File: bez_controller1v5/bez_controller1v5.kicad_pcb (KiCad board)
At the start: 4 copper layers, 110 x 65 mm, 88 parts, among them J1 Conn_01x03_Male, J10 Conn_01x07_Socket, J11 Conn_01x03_Male, J12 Conn_01x03_Male, J13 USB_B_Mini, J14 PPTC041LGBN-RC, J15 Conn_01x03_Male, J16 MOLEX_Conn_Button, J17 MOLEX_Conn_Button, J2 Conn_01x03_Male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

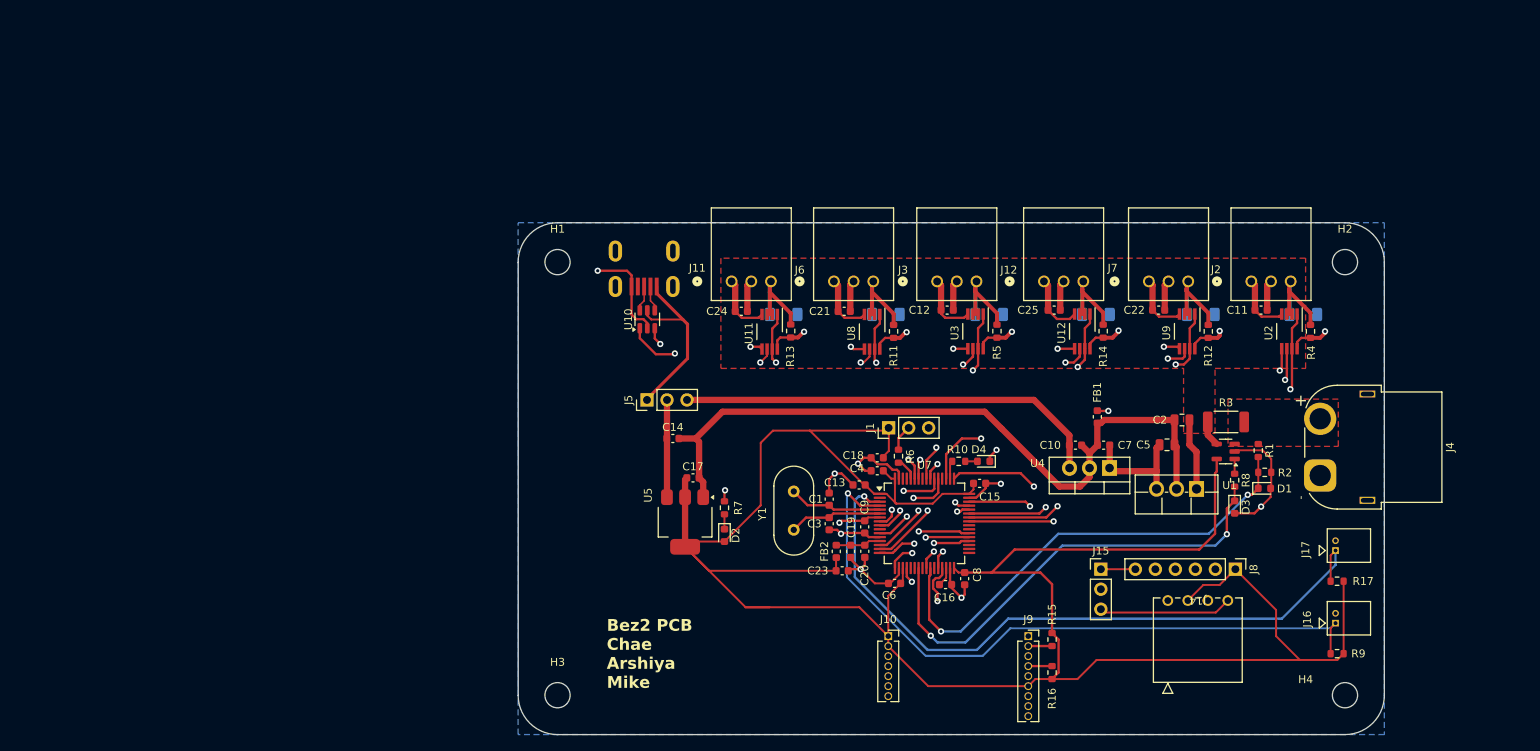
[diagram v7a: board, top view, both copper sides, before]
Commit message: -added label on each motor connections, -thickened 3.3v wires, removed uart line squiggles, updated U1 12v to 6v dcdc converter to new pxo7806-500
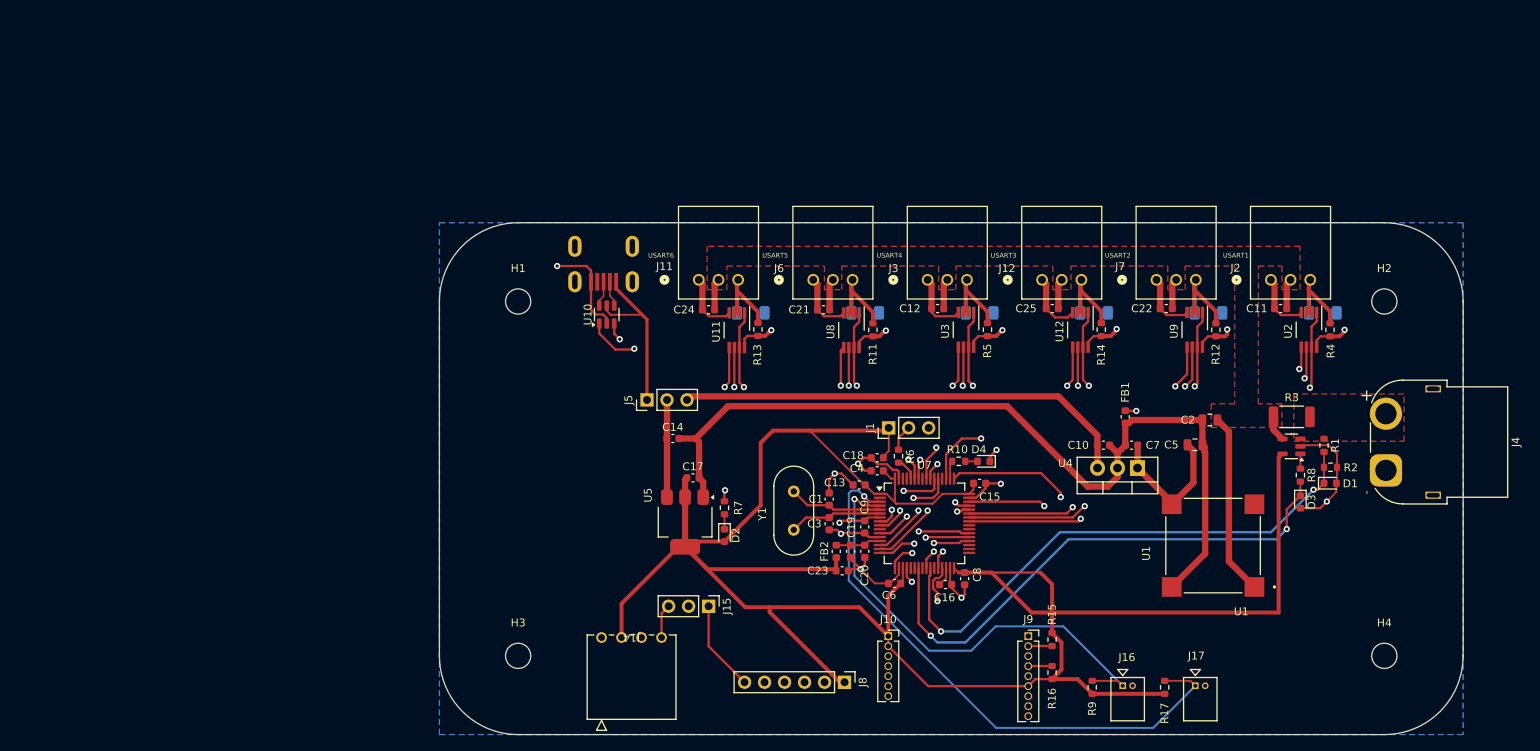
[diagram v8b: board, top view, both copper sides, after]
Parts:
- U1: value PX07806-500-S -> ~; footprint Package_TO_SOT_THT:TO-220F-3_Vertical -> KiCad:CONV_PXO7806-500-M-TR
- moved J14 72.1 mm to (104.3, 95.7)
- moved J8 51.7 mm to (135.2, 101.3)
- moved J15 50.0 mm to (117.9, 91.7), turned to -90 degrees
- moved R9 31.4 mm to (166.7, 102.0), turned to 90 degrees
- moved J16 28.2 mm to (170.5, 101.8), turned to 0 degrees
- moved R17 25.7 mm to (175.8, 102.0), turned to 90 degrees
- moved J17 24.7 mm to (179.8, 101.8), turned to 0 degrees
- moved R3 8.38 mm to (192.0, 67.7)
- moved D1 8.38 mm to (196.9, 76.1)
- moved D3 8.38 mm to (193.1, 78.5)
- moved J4 8.38 mm to (203.9, 74.5)
- moved R1 8.38 mm to (196.1, 71.3)
- moved R2 8.38 mm to (196.9, 74.0)
- moved R8 8.38 mm to (193.1, 75.0)
- moved U6 8.38 mm to (191.9, 71.4)
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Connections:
- U1 pad 2: /PWR_GND -> (no net)
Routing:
- net /GPIO1: track 87.4 -> 60.0 mm
- net /NRST: track 55.2 -> 29.6 mm
- net /TMS: track 31.3 -> 52.5 mm
- net /Screen_SCL: track 42.5 -> 61.3 mm
- net /PWR_GND: track 93.4 -> 111.7 mm
- net /TCK: track 41.0 -> 56.2 mm
- net /GPIO2: track 88.8 -> 73.9 mm
- net /post_shunt_12v: track 35.7 -> 49.8 mm
- net /SWO_or_Screen_SDA: track 32.7 -> 45.5 mm
- net /Screen_SDA: track 16.9 -> 4.35 mm
- net /V_bat_read: track 60.5 -> 69.1 mm
- net /V_shunt_read: track 59.3 -> 67.5 mm
- net /SWO: track 4.38 -> 11.5 mm
- net +3.3V: track 306.3 -> 299.7 mm
- net /USB_D+: track 58.0 -> 63.4 mm
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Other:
- board size 110 x 65 mm -> 130 x 65 mm
- board text added: "U1"
- board text added: "USART1"
- board text added: "USART2"
- board text added: "USART3"
- board text added: "USART4"
- board text added: "USART5"
- board text added: "USART6"
- board text removed: "Bez2 PCB Chae Arshiya Mike"
